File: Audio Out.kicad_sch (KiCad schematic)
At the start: 18 parts

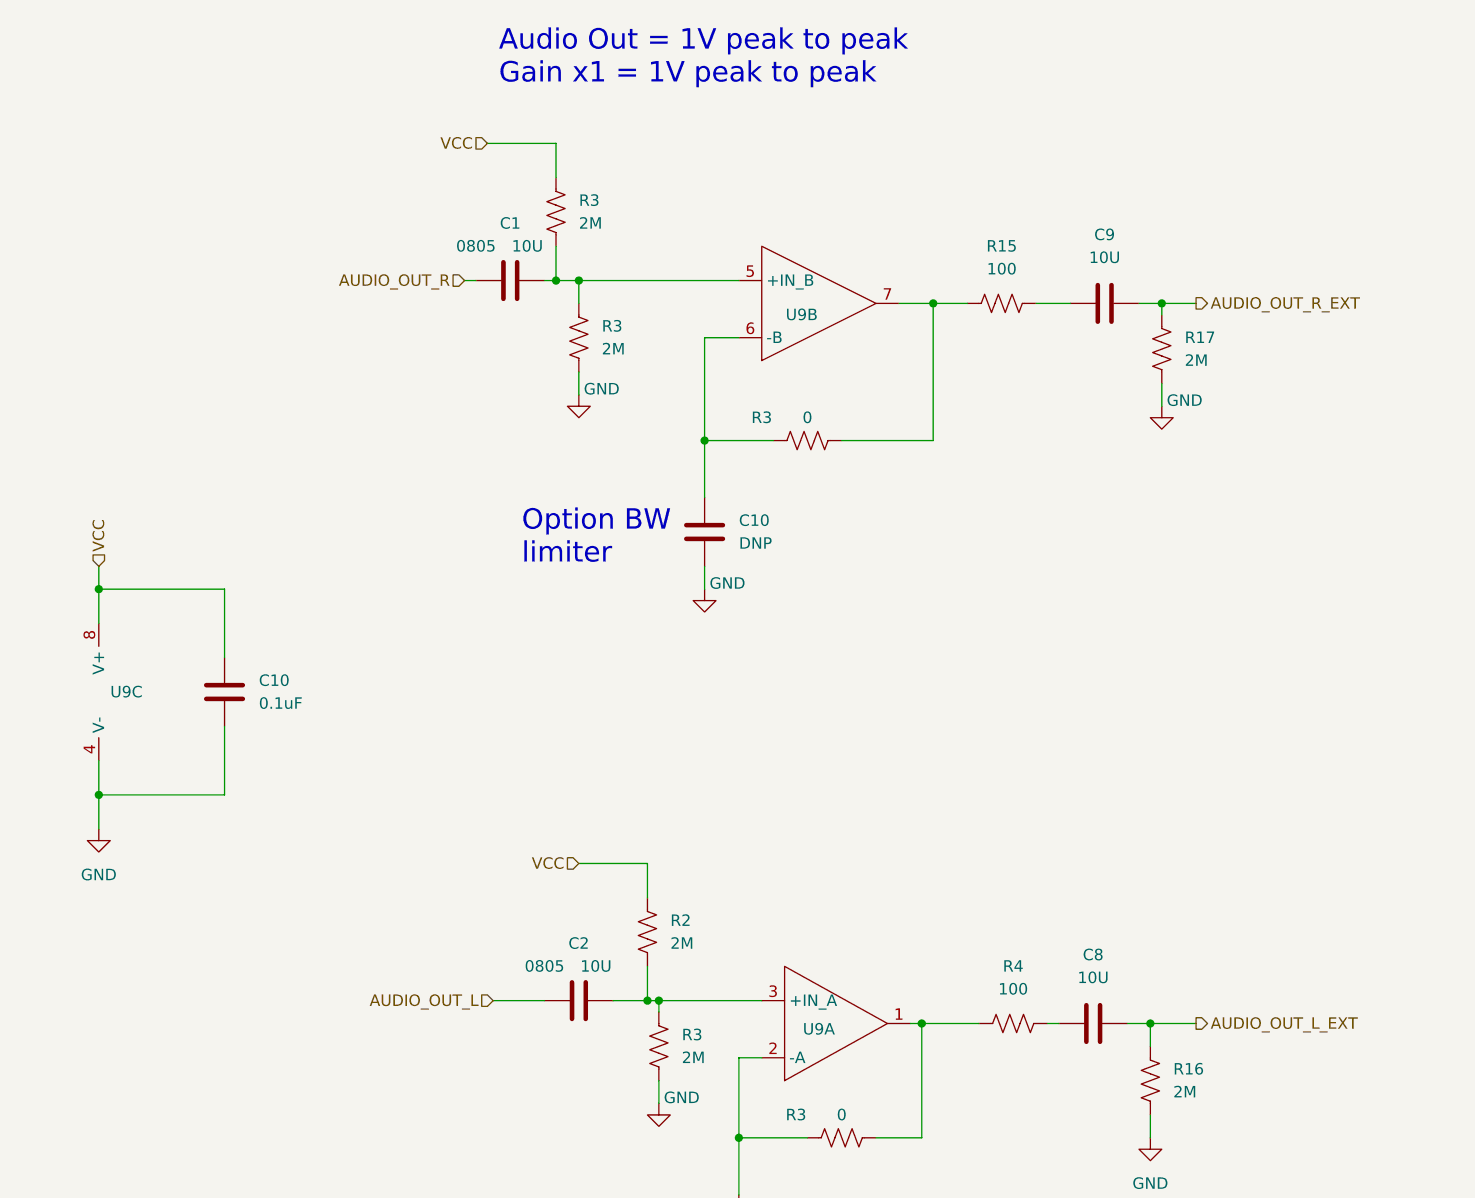
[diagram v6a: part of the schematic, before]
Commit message: added dedicated SPI, UART, I2C connectors
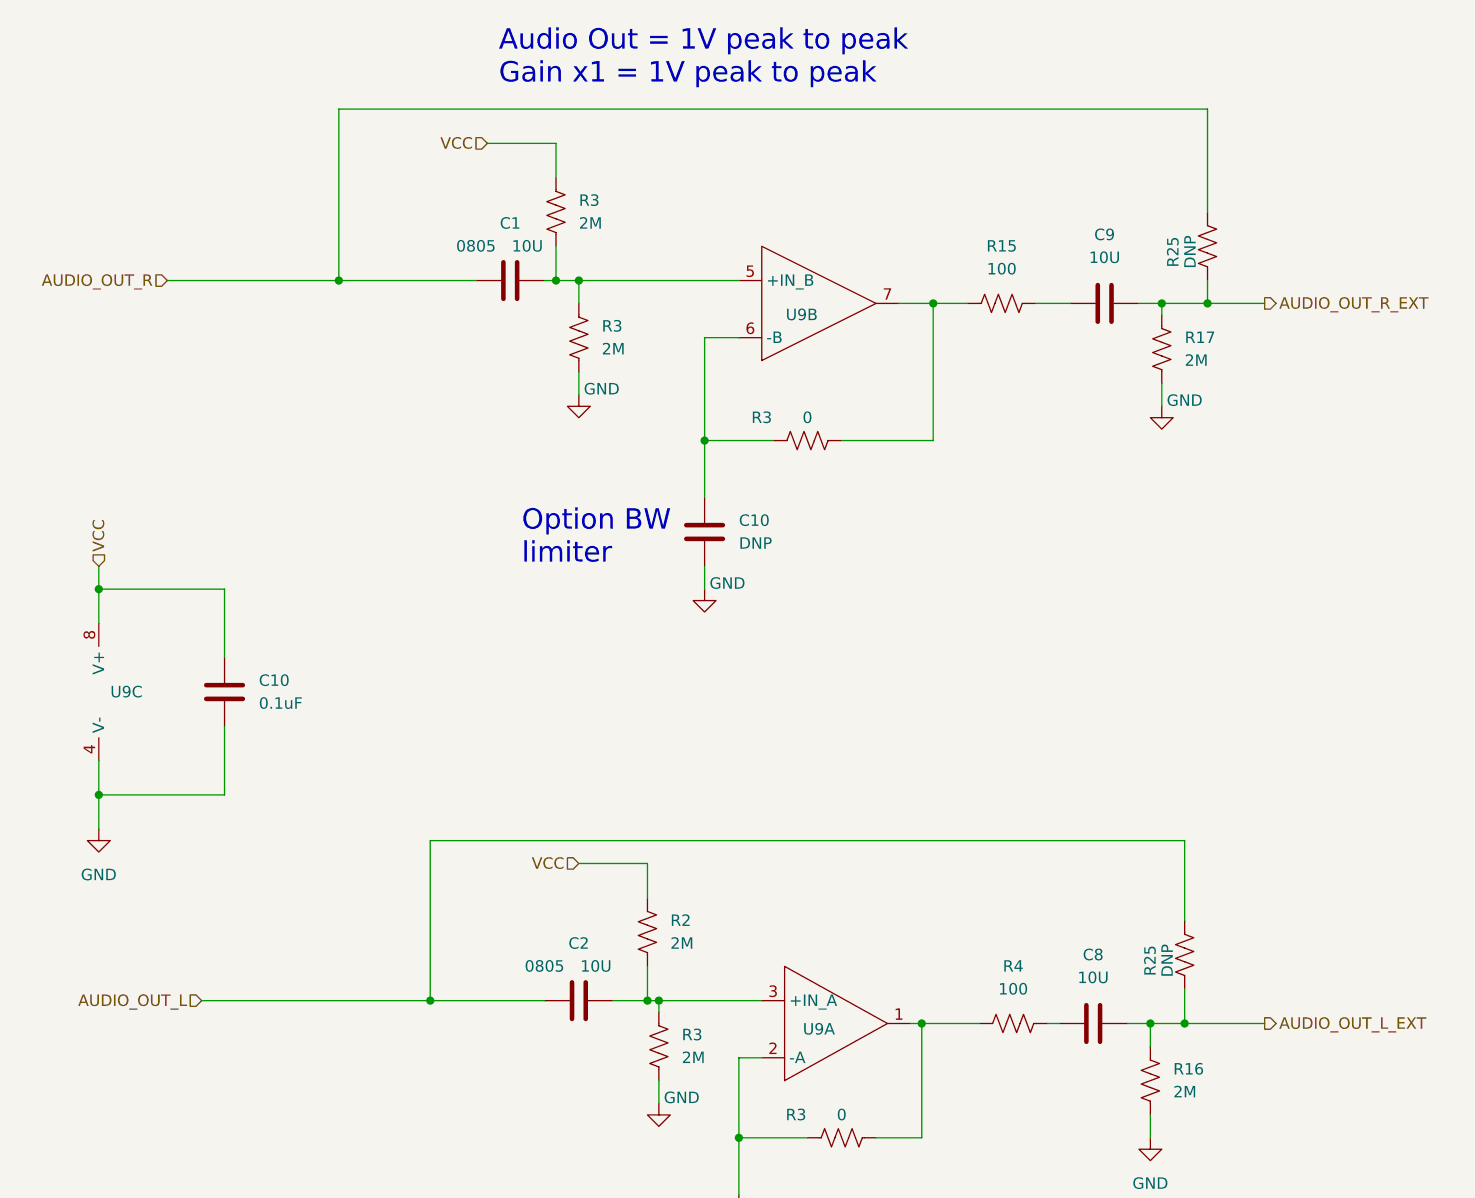
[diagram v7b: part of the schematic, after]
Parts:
- added R25 (x2): DNP, Resistor_SMD:R_0402_1005Metric, symbol Device:R_US
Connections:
- net AUDIO_OUT_L: now also R25.2
- net AUDIO_OUT_L_EXT: now also R25.1
- net AUDIO_OUT_R: now also R25.2
- net AUDIO_OUT_R_EXT: now also R25.1
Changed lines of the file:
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@@
 (kicad_sch (version 20230121) (generator eeschema)
   (paper "A4")
+  (junction (at 91.44 130.81) (diameter 0) (color 0 0 0 0)
+  )
   (junction (at 146.05 133.35) (diameter 0) (color 0 0 0 0)
   )
   (junction (at 116.84 130.81) (diameter 0) (color 0 0 0 0)
   )
+  (junction (at 81.28 50.8) (diameter 0) (color 0 0 0 0)
+  )
   (junction (at 54.61 85.09) (diameter 0) (color 0 0 0 0)
   )
   (junction (at 171.45 133.35) (diameter 0) (color 0 0 0 0)
   )
+  (junction (at 177.8 53.34) (diameter 0) (color 0 0 0 0)
+  )
   (junction (at 115.57 130.81) (diameter 0) (color 0 0 0 0)
   )
+  (junction (at 175.26 133.35) (diameter 0) (color 0 0 0 0)
+  )
   (junction (at 172.72 53.34) (diameter 0) (color 0 0 0 0)
   )
@@
     (stroke (width 0) (type default))
   )
+  (wire (pts (xy 81.28 50.8) (xy 96.52 50.8))
+    (stroke (width 0) (type default))
+  )
   (wire (pts (xy 54.61 107.95) (xy 54.61 104.14))
     (stroke (width 0) (type default))
@@
     (stroke (width 0) (type default))
   )
+  (wire (pts (xy 175.26 129.54) (xy 175.26 133.35))
+    (stroke (width 0) (type default))
+  )
   (wire (pts (xy 97.79 35.56) (xy 105.41 35.56))
     (stroke (width 0) (type default))
@@
     (stroke (width 0) (type default))
   )
+  (wire (pts (xy 91.44 130.81) (xy 104.14 130.81))
+    (stroke (width 0) (type default))
+  )
   (wire (pts (xy 125.73 162.56) (xy 125.73 160.02))
     (stroke (width 0) (type default))
@@
     (stroke (width 0) (type default))
   )
-  (wire (pts (xy 98.425 130.81) (xy 104.14 130.81))
+  (wire (pts (xy 66.04 130.81) (xy 91.44 130.81))
+    (stroke (width 0) (type default))
+  )
+  (wire (pts (xy 177.8 53.34) (xy 172.72 53.34))
     (stroke (width 0) (type default))
   )
@@
     (stroke (width 0) (type default))
   )
-  (wire (pts (xy 95.25 50.8) (xy 96.52 50.8))
+  (wire (pts (xy 62.23 50.8) (xy 81.28 50.8))
     (stroke (width 0) (type default))
   )
@@
     (stroke (width 0) (type default))
   )
+  (wire (pts (xy 175.26 133.35) (xy 171.45 133.35))
+    (stroke (width 0) (type default))
+  )
   (wire (pts (xy 171.45 133.35) (xy 171.45 135.89))
     (stroke (width 0) (type default))
   )
-  (wire (pts (xy 176.53 133.35) (xy 171.45 133.35))
-    (stroke (width 0) (type default))
-  )
-  (wire (pts (xy 176.53 53.34) (xy 172.72 53.34))
+  (wire (pts (xy 184.15 133.35) (xy 175.26 133.35))
+    (stroke (width 0) (type default))
+  )
+  (wire (pts (xy 184.15 53.34) (xy 177.8 53.34))
     (stroke (width 0) (type default))
   )
@@
     (stroke (width 0) (type default))
   )
+  (wire (pts (xy 91.44 113.03) (xy 91.44 130.81))
+    (stroke (width 0) (type default))
+  )
   (wire (pts (xy 171.45 133.35) (xy 168.91 133.35))
     (stroke (width 0) (type default))
   )
+  (wire (pts (xy 177.8 43.18) (xy 177.8 31.75))
+    (stroke (width 0) (type default))
+  )
   (wire (pts (xy 116.84 130.81) (xy 116.84 132.08))
     (stroke (width 0) (type default))
   )
+  (wire (pts (xy 177.8 50.8) (xy 177.8 53.34))
+    (stroke (width 0) (type default))
+  )
+  (wire (pts (xy 175.26 121.92) (xy 175.26 113.03))
+    (stroke (width 0) (type default))
+  )
   (wire (pts (xy 115.57 130.81) (xy 116.84 130.81))
     (stroke (width 0) (type default))
@@
     (stroke (width 0) (type default))
   )
+  (wire (pts (xy 177.8 31.75) (xy 81.28 31.75))
+    (stroke (width 0) (type default))
+  )
   (wire (pts (xy 68.58 85.09) (xy 54.61 85.09))
     (stroke (width 0) (type default))
@@
     (stroke (width 0) (type default))
   )
+  (wire (pts (xy 81.28 31.75) (xy 81.28 50.8))
+    (stroke (width 0) (type default))
+  )
   (wire (pts (xy 125.73 137.16) (xy 125.73 146.05))
     (stroke (width 0) (type default))
   )
   (wire (pts (xy 54.61 111.76) (xy 54.61 107.95))
+    (stroke (width 0) (type default))
+  )
+  (wire (pts (xy 175.26 113.03) (xy 91.44 113.03))
     (stroke (width 0) (type default))
   )
@@
     (effects (font (size 2.27 2.27)) (justify left bottom))
   )
-  (hierarchical_label "AUDIO_OUT_L" (shape input) (at 98.425 130.81 180) (fields_autoplaced)
+  (hierarchical_label "AUDIO_OUT_L" (shape input) (at 66.04 130.81 180) (fields_autoplaced)
     (effects (font (size 1.27 1.27)) (justify right))
   )
@@
     (effects (font (size 1.27 1.27)) (justify left))
   )
-  (hierarchical_label "AUDIO_OUT_L_EXT" (shape output) (at 176.53 133.35 0) (fields_autoplaced)
+  (hierarchical_label "AUDIO_OUT_L_EXT" (shape output) (at 184.15 133.35 0) (fields_autoplaced)
     (effects (font (size 1.27 1.27)) (justify left))
   )
-  (hierarchical_label "AUDIO_OUT_R_EXT" (shape output) (at 176.53 53.34 0) (fields_autoplaced)
+  (hierarchical_label "AUDIO_OUT_R_EXT" (shape output) (at 184.15 53.34 0) (fields_autoplaced)
     (effects (font (size 1.27 1.27)) (justify left))
   )
@@
     (effects (font (size 1.27 1.27)) (justify right))
   )
-  (hierarchical_label "AUDIO_OUT_R" (shape input) (at 95.25 50.8 180) (fields_autoplaced)
+  (hierarchical_label "AUDIO_OUT_R" (shape input) (at 62.23 50.8 180) (fields_autoplaced)
     (effects (font (size 1.27 1.27)) (justify right))
   )
@@
     )
   )
+  (symbol (lib_id "Device:R_US") (at 175.26 125.73 180) (unit 1)
+    (in_bom yes) (on_board yes) (dnp no)
+    (property "Reference" "R25" (at 171.45 126.365 90)
+      (effects (font (size 1.27 1.27)))
+    )
+    (property "Value" "DNP" (at 173.355 126.365 90)
+      (effects (font (size 1.27 1.27)))
+    )
+    (property "Footprint" "Resistor_SMD:R_0402_1005Metric" (at 174.244 125.476 90)
+      (effects (font (size 1.27 1.27)) hide)
+    )
+    (property "Datasheet" "~" (at 175.26 125.73 0)
+      (effects (font (size 1.27 1.27)) hide)
+    )
+    (property "Specks" "0402" (at 173.355 129.54 90)
+      (effects (font (size 1.27 1.27)) hide)
+    )
+    (pin "1")
+    (pin "2")
+    (instances
+      (project "DaisySeedBreakout"
+        (path "/a83c9f4b-f61b-47d4-b39d-4636bff6eb0e"
+          (reference "R25") (unit 1)
+        )
+        (path "/a83c9f4b-f61b-47d4-b39d-4636bff6eb0e/a0f8a1fd-6189-4b02-8cf7-e8d7538f4e50"
+          (reference "R26") (unit 1)
+        )
+        (path "/a83c9f4b-f61b-47d4-b39d-4636bff6eb0e/d5f93f74-350a-43ef-bdfb-299723239788"
+          (reference "R29") (unit 1)
+        )
+      )
+    )
+  )
   (symbol (lib_id "power:GND") (at 116.84 142.24 0) (unit 1)
     (in_bom yes) (on_board yes) (dnp no)
@@
         )
       )
+    )
+  )
+  (symbol (lib_id "Device:R_US") (at 177.8 46.99 180) (unit 1)
+    (in_bom yes) (on_board yes) (dnp no)
+    (property "Reference" "R25" (at 173.99 47.625 90)
+      (effects (font (size 1.27 1.27)))
+    )
+    (property "Value" "DNP" (at 175.895 47.625 90)
+      (effects (font (size 1.27 1.27)))
+    )
+    (property "Footprint" "Resistor_SMD:R_0402_1005Metric" (at 176.784 46.736 90)
+      (effects (font (size 1.27 1.27)) hide)
+    )
+    (property "Datasheet" "~" (at 177.8 46.99 0)
+      (effects (font (size 1.27 1.27)) hide)
+    )
+    (property "Specks" "0402" (at 175.895 50.8 90)
+      (effects (font (size 1.27 1.27)) hide)
+    )
+    (pin "1")
+    (pin "2")
+    (instances
+      (project "DaisySeedBreakout"
+        (path "/a83c9f4b-f61b-47d4-b39d-4636bff6eb0e"
+          (reference "R25") (unit 1)
+        )
+        (path "/a83c9f4b-f61b-47d4-b39d-4636bff6eb0e/a0f8a1fd-6189-4b02-8cf7-e8d7538f4e50"
+          (reference "R26") (unit 1)
+        )
+        (path "/a83c9f4b-f61b-47d4-b39d-4636bff6eb0e/d5f93f74-350a-43ef-bdfb-299723239788"
+          (reference "R28") (unit 1)
+        )
+      )

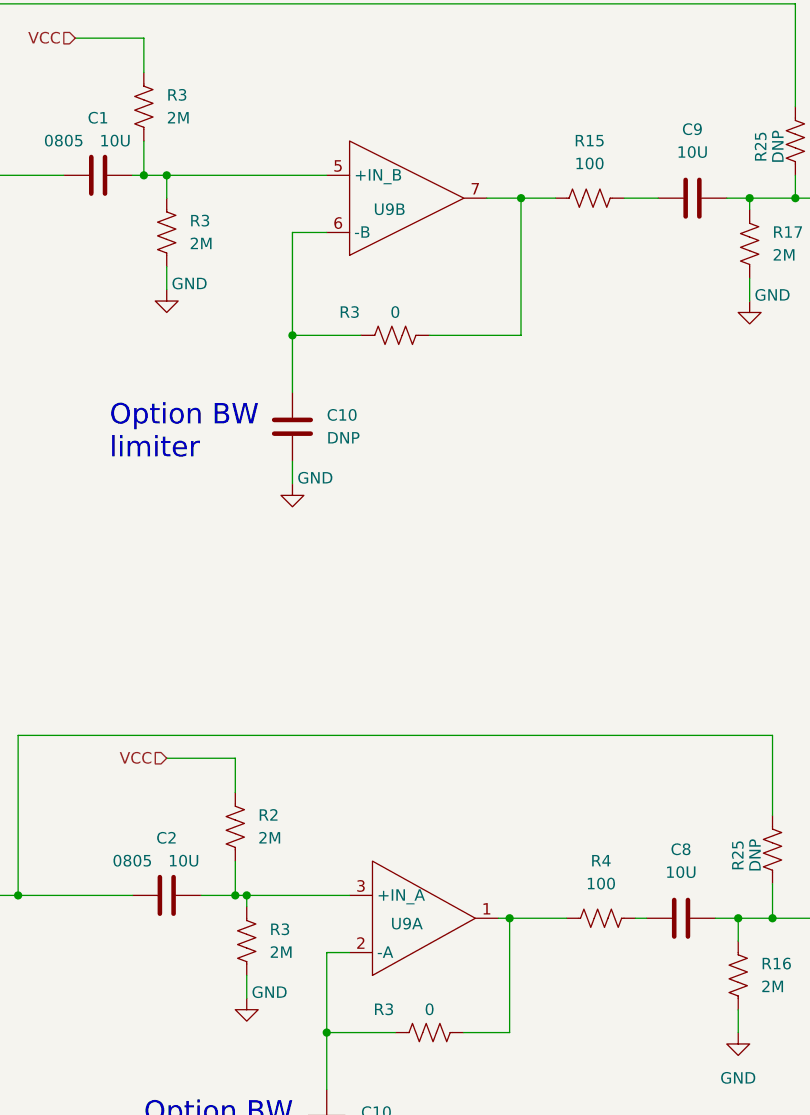
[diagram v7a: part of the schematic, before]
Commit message: PCB cleanup, added accelerometer as easy sensor to begin with
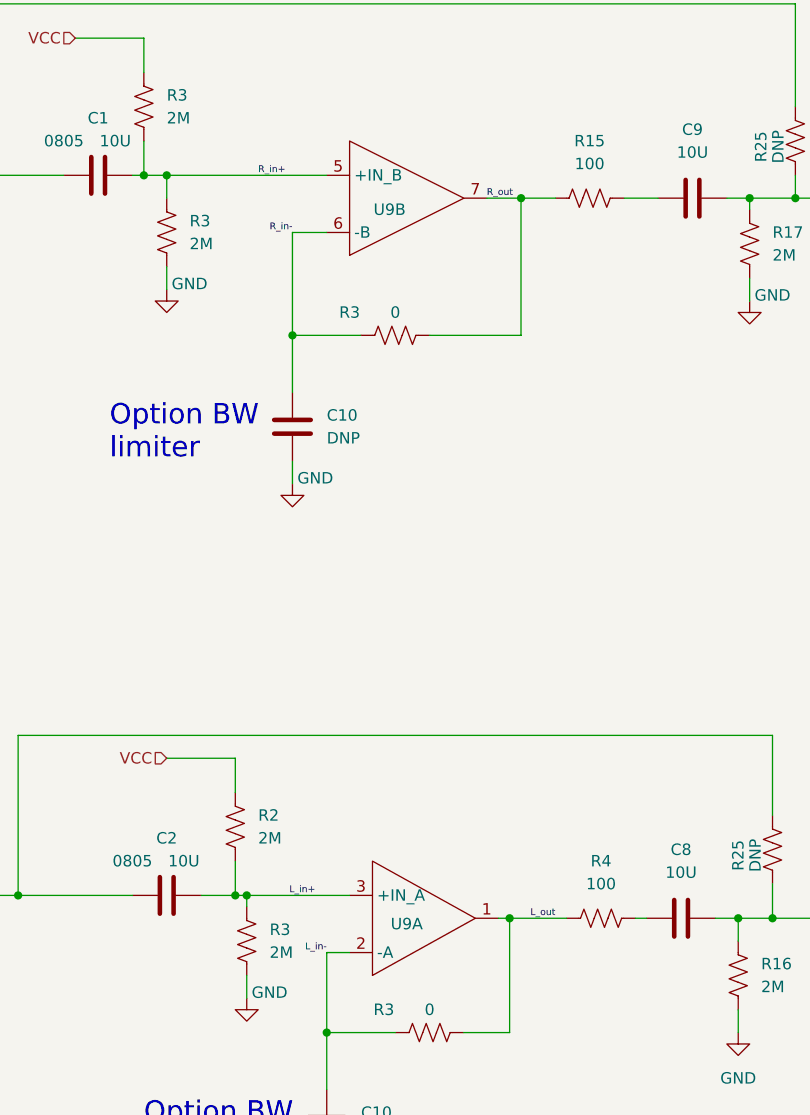
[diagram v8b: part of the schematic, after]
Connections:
- net R_in+: now reaches C1.2, R3.1, R3.2, U9.5 (+IN_B)
- net R_in-: now reaches C10.1, R3.1, U9.6 (-B)
- net R_out: now reaches R15.1, R3.2, U9.7
- net L_in-: now reaches C10.1, R3.1, U9.2 (-A)
- net L_out: now reaches R3.2, R4.1, U9.1
- net L_in+: now reaches C2.2, R2.2, R3.1, U9.3 (+IN_A)
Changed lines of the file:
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@@
+    (stroke (width 0) (type default))
+  )
+  (wire (pts (xy 143.51 53.34) (xy 147.32 53.34))
     (stroke (width 0) (type default))
   )
@@
     (stroke (width 0) (type default))
   )
-  (wire (pts (xy 121.92 68.58) (xy 121.92 57.15))
+  (wire (pts (xy 121.92 57.15) (xy 121.92 68.58))
+    (stroke (width 0) (type default))
+  )
+  (wire (pts (xy 107.95 50.8) (xy 125.73 50.8))
     (stroke (width 0) (type default))
   )
@@
     (stroke (width 0) (type default))
   )
-  (wire (pts (xy 107.95 50.8) (xy 125.73 50.8))
-    (stroke (width 0) (type default))
-  )
   (wire (pts (xy 91.44 113.03) (xy 91.44 130.81))
     (stroke (width 0) (type default))
@@
   )
   (wire (pts (xy 68.58 92.71) (xy 68.58 85.09))
-    (stroke (width 0) (type default))
-  )
-  (wire (pts (xy 143.51 53.34) (xy 147.32 53.34))
     (stroke (width 0) (type default))
   )
@@
     (effects (font (size 2.27 2.27)) (justify left bottom))
   )
+  (label "L_in-" (at 125.73 137.16 180) (fields_autoplaced)
+    (effects (font (size 0.75 0.75)) (justify right bottom))
+  )
+  (label "R_in+" (at 118.11 50.8 0) (fields_autoplaced)
+    (effects (font (size 0.75 0.75)) (justify left bottom))
+  )
+  (label "R_in-" (at 121.92 57.15 180) (fields_autoplaced)
+    (effects (font (size 0.75 0.75)) (justify right bottom))
+  )
+  (label "L_in+" (at 124.46 130.81 180) (fields_autoplaced)
+    (effects (font (size 0.75 0.75)) (justify right bottom))
+  )
+  (label "L_out" (at 151.13 133.35 180) (fields_autoplaced)
+    (effects (font (size 0.75 0.75)) (justify right bottom))
+  )
+  (label "R_out" (at 143.51 53.34 0) (fields_autoplaced)
+    (effects (font (size 0.75 0.75)) (justify left bottom))
+  )
   (hierarchical_label "AUDIO_OUT_L" (shape input) (at 66.04 130.81 180) (fields_autoplaced)
